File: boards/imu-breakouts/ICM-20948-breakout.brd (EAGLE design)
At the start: 15.2 x 12.7 mm, 7 parts, among them U1 ICM-20948, U3 ICM-42605

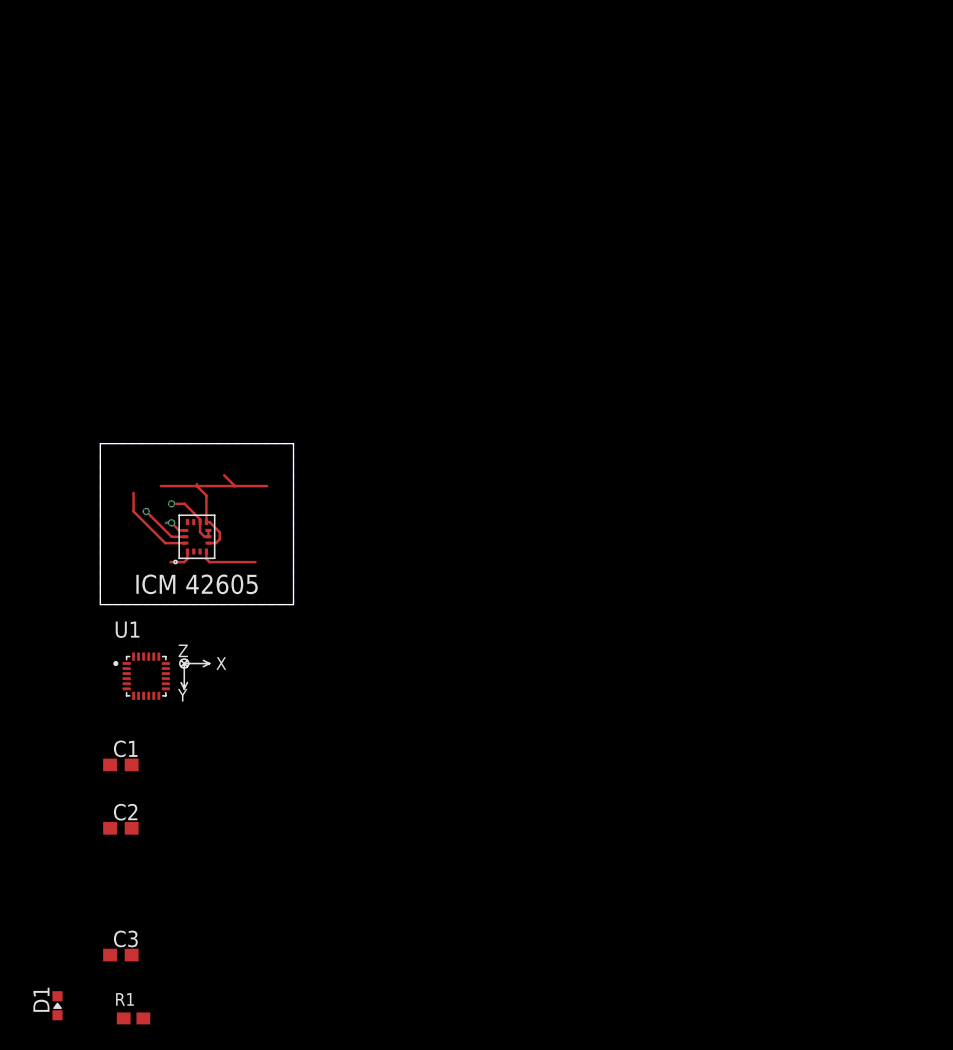
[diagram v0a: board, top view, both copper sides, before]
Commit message: updated icm20948 breakout
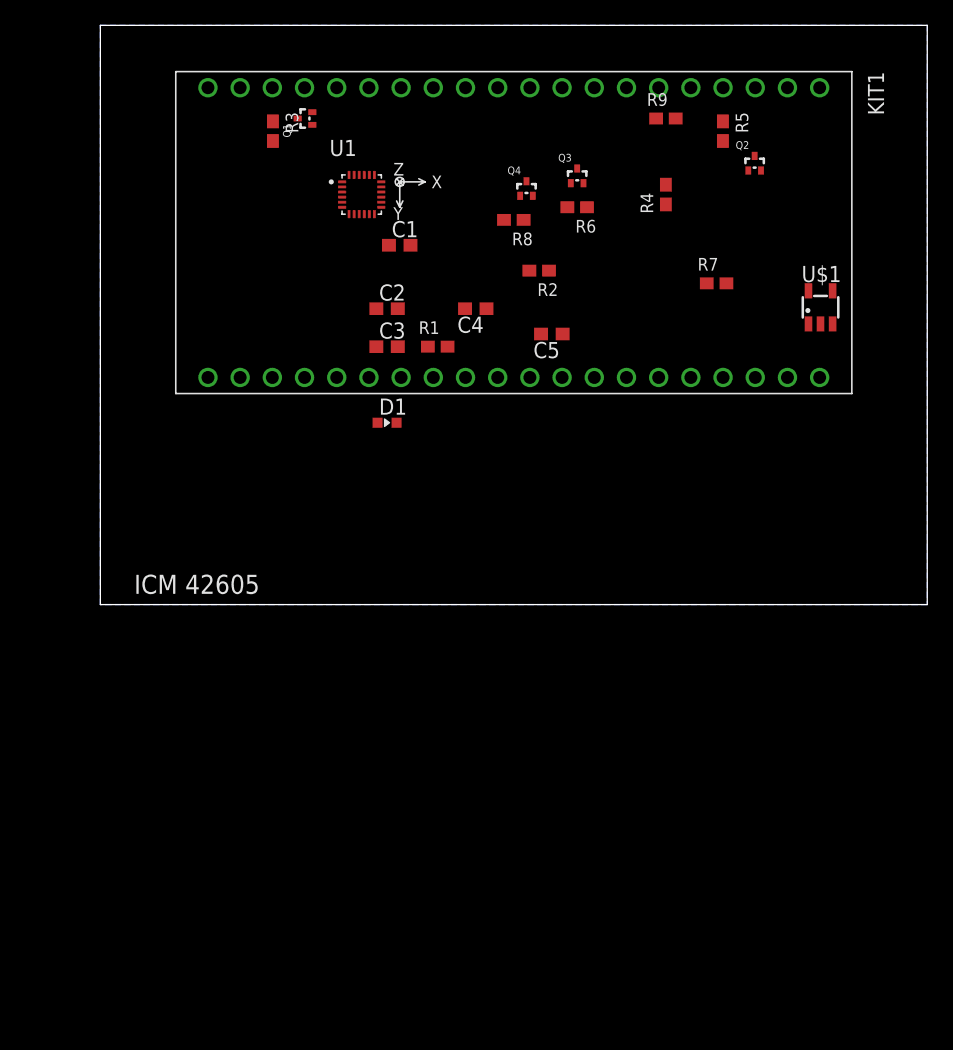
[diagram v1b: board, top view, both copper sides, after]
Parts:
- removed U3: ICM-42605, RoboJackets-Sensors:ICM-442605-2530091
- added C4, C5: 1uF, rcl:C0603
- added KIT1: MTRAIN, RoboJackets-Boards:MTRAIN-KIT
- added Q1, Q2, Q3, Q4: 20V/0.2A/8MHz/1.2Ω/1Vth, SparkFun-DiscreteSemi:SOT-416FL
- added R2, R3, R4, R5, R6, R7, R8, R9: 2.2k, RoboJackets-Resistors:R0603W
- added U$1: NCP161, RoboJackets-PowerICs:SOT-23-5
- moved R1 58.2 mm to (19.0, 14.0)
- moved D1 52.8 mm to (15.0, 8.00), turned to 270 degrees
- moved C3 52.4 mm to (15.0, 14.0)
- moved C1 46.5 mm to (16.0, 22.0)
- moved C2 46.1 mm to (15.0, 17.0)
- moved U1 41.6 mm to (13.0, 26.0)
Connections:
- net N$2 renamed REGOUT
- removed net INT: U3.P$4
- new net !CS!_VIN: KIT1.P$18, Q1.3, R3.1
- new net +5.0V: KIT1.VDD
- new net CLK_VIN: KIT1.P$6, Q4.3, R9.1
- new net MISO_VIN: KIT1.P$5, Q3.3, R7.1
- new net MOSI_VIN: KIT1.P$4, Q2.3, R5.1
- new net VBUS: KIT1.VBUS
- new net VIN: KIT1.VIN
- net !CS!: now also Q1.2, Q2.2, R2.1, R4.1; no longer U3.P$12
- net +1.8V: now also C4.1, Q1.1, Q2.1, Q3.1, Q4.1, R2.2, R4.2, R6.2, R8.2, U$1.5
- net +3.3V: now also C5.1, R3.2, R5.2, R7.2, R9.2, U$1.1, U$1.3; no longer U3.P$5, U3.P$8
- net CLK: now also Q4.2, R8.1; no longer U3.P$13
- net GND: now also C4.2, C5.2, KIT1.GND, U$1.2, U1.11; no longer U3.P$6, U3.P$7, U3.P$9
- net MISO: now also Q3.2, R6.1; no longer U3.P$1
- net MOSI: no longer U3.P$14
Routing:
- net +3.3V: track 15.8 -> 0.00 mm
- net MOSI: track 6.58 -> 0.00 mm
- net GND: track 5.08 -> 0.00 mm, vias 1 -> 0
- net INT: track 4.56 -> 0.00 mm
- net CLK: track 4.00 -> 0.00 mm, vias 1 -> 0
- net MISO: track 2.02 -> 0.00 mm
- net !CS!: track 1.78 -> 0.00 mm, vias 1 -> 0
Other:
- board size 15.2 x 12.7 mm -> 65.2 x 45.7 mm

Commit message: added ICM 20948 breakout
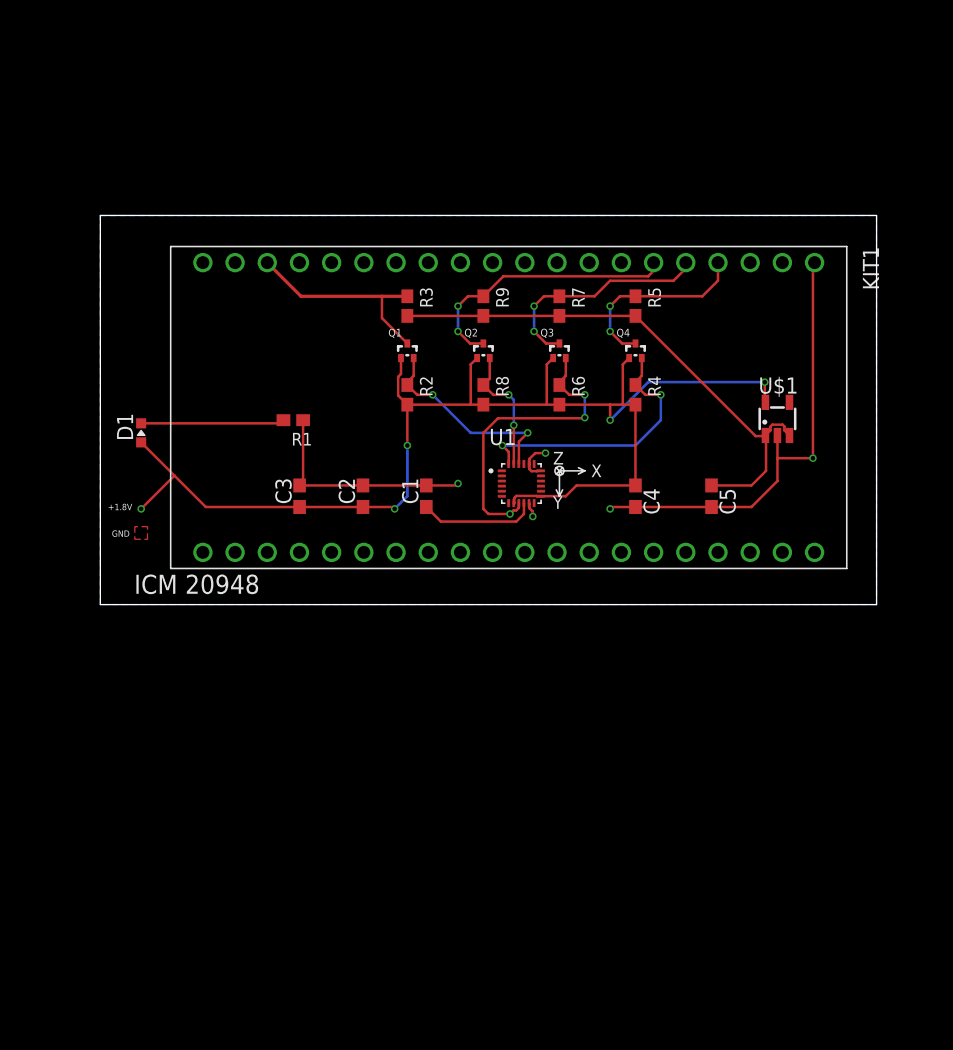
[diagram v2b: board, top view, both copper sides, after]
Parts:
- moved U1 26.0 mm to (25.6, 3.20)
- moved Q2 26.0 mm to (22.6, 14.2)
- moved R9 20.6 mm to (22.6, 17.2), turned to 270 degrees
- moved C1 19.9 mm to (18.1, 2.20), turned to 90 degrees
- moved Q1 19.8 mm to (16.6, 14.2), turned to 0 degrees
- moved C4 19.4 mm to (34.6, 2.20), turned to 270 degrees
- moved D1 19.4 mm to (-4.40, 7.20), turned to 0 degrees
- moved C5 18.0 mm to (40.6, 2.20), turned to 270 degrees
- moved R3 17.4 mm to (16.6, 17.2)
- moved R4 16.0 mm to (34.6, 10.2), turned to 270 degrees
- moved R5 15.4 mm to (34.6, 17.2)
- moved Q4 15.4 mm to (34.6, 14.2)
- moved C2 14.9 mm to (13.1, 2.20), turned to 90 degrees
- moved R6 14.9 mm to (28.6, 10.2), turned to 270 degrees
- moved R2 14.3 mm to (16.6, 10.2), turned to 270 degrees
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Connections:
- net !CS!: no longer Q2.2, R4.1
- net CLK: now also Q2.2; no longer Q4.2
- net CLK_VIN: now also Q2.3; no longer Q4.3
- net MOSI: now also Q4.2, R4.1
- net MOSI_VIN: now also Q4.3; no longer Q2.3
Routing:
- net +1.8V: track 0.00 -> 101.4 mm, vias 0 -> 5
- net GND: track 0.00 -> 58.3 mm, vias 0 -> 5
- net +3.3V: track 0.00 -> 42.8 mm
- net MISO: track 0.00 -> 24.5 mm, vias 0 -> 3
- net MOSI: track 0.00 -> 21.6 mm, vias 0 -> 2
- net CLK_VIN: track 0.00 -> 21.6 mm, vias 0 -> 2
- net MISO_VIN: track 0.00 -> 18.1 mm, vias 0 -> 2
- net !CS!_VIN: track 0.00 -> 16.7 mm
- net !CS!: track 0.00 -> 16.1 mm, vias 0 -> 2
- net MOSI_VIN: track 0.00 -> 15.2 mm, vias 0 -> 2
- net N$1: track 0.00 -> 11.3 mm
- net CLK: track 0.00 -> 10.3 mm, vias 0 -> 2
- net REGOUT: track 0.00 -> 9.29 mm
- added copper zone on layer 1, net GND
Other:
- board size 65.2 x 45.7 mm -> 61.2 x 30.7 mm
- board text added: "+1.8V"
- board text added: "2020"
- board text added: "GND"
- board text added: "ICM 20948"
- board text removed: "2019"
- board text removed: "ICM 42605"
